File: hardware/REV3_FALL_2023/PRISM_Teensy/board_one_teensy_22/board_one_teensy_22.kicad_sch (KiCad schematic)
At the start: 20 parts, among them J2 PRISM_IO_INTERFACE, J3 3387, U1 Teensy4.0, U2 GPS-14414, U3 3966, U4 RFM69HCW_Breakout

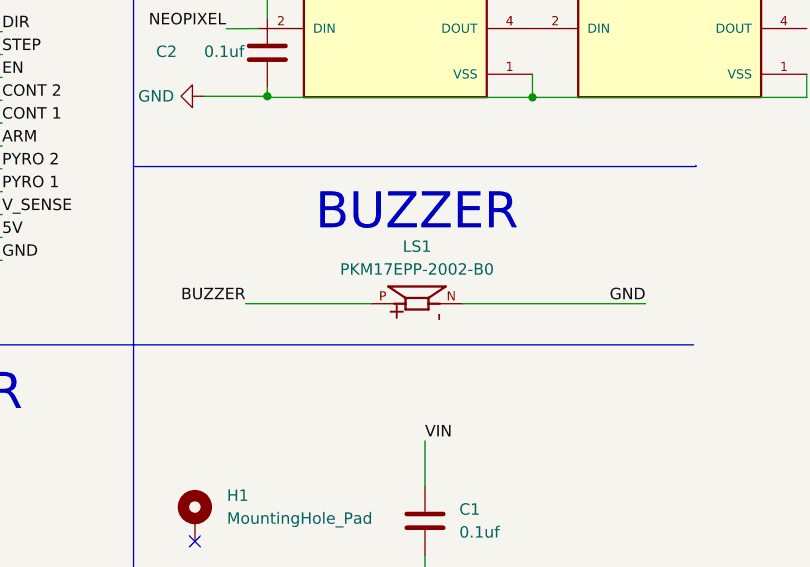
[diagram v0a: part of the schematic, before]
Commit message: created new symbol and footprint for buzzer
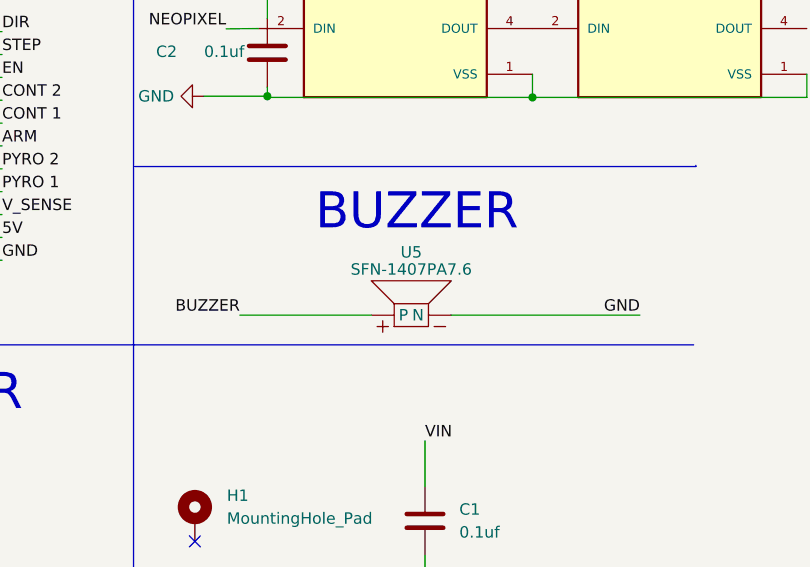
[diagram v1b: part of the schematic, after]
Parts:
- removed LS1: PKM17EPP-2002-B0, PKM17EPP-2002-B0:SPKR_PKM17EPP-2002-B0, symbol PKM:PKM17EPP-2002-B0
- added U5: SFN-1407PA7.6, buzzers:SFN-1407PA7.6, symbol SFN-1407PA7.6:SFN-1407PA7.6
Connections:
- net BUZZER: now also U5. (P)
- net GND: now also U5. (P)
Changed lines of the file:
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@@
     (stroke (width 0) (type default))
   )
-  (wire (pts (xy 279.4 66.04) (xy 259.08 66.04))
+  (wire (pts (xy 257.81 67.31) (xy 278.765 67.31))
     (stroke (width 0) (type default))
   )
@@
     (stroke (width 0) (type default))
   )
-  (wire (pts (xy 234.95 66.04) (xy 248.92 66.04))
+  (wire (pts (xy 234.315 67.31) (xy 248.92 67.31))
     (stroke (width 0) (type default))
   )
@@
     (effects (font (size 1.27 1.27)) (justify right bottom))
   )
-  (label "BUZZER" (at 234.95 66.04 180) (fields_autoplaced)
+  (label "BUZZER" (at 234.315 67.31 180) (fields_autoplaced)
     (effects (font (size 1.27 1.27)) (justify right bottom))
   )
@@
     (effects (font (size 1.27 1.27)) (justify left bottom))
   )
-  (label "GND" (at 279.4 66.04 180) (fields_autoplaced)
+  (label "GND" (at 278.765 67.31 180) (fields_autoplaced)
     (effects (font (size 1.27 1.27)) (justify right bottom))
   )
@@
         (path "/7a48c3b0-2761-409e-ae2f-7ebae3820225"
           (reference "D5") (unit 1)
+        )
+      )
+    )
+  )
+  (symbol (lib_id "SFN-1407PA7.6:SFN-1407PA7.6") (at 253.365 64.77 0) (unit 1)
+    (in_bom yes) (on_board yes) (dnp no)
+    (property "Reference" "U5" (at 253.365 60.325 0)
+      (effects (font (size 1.27 1.27)))
+    )
+    (property "Value" "SFN-1407PA7.6" (at 253.365 62.23 0)
+      (effects (font (size 1.27 1.27)))
+    )
+    (property "Footprint" "buzzers:SFN-1407PA7.6" (at 251.46 67.31 90)
+      (effects (font (size 1.27 1.27)) hide)
+    )
+    (property "Datasheet" "" (at 251.46 67.31 90)
+      (effects (font (size 1.27 1.27)) hide)
+    )
+    (pin "")
+    (pin "")
+    (instances
+      (project "board_one_teensy_22"
+        (path "/7a48c3b0-2761-409e-ae2f-7ebae3820225"
+          (reference "U5") (unit 1)
         )
       )
@@
         )
       )
-    )
-  )
-  (symbol (lib_id "PKM:PKM17EPP-2002-B0") (at 254 66.04 90) (unit 1)
-    (in_bom yes) (on_board yes) (dnp no) (fields_autoplaced)
-    (property "Reference" "LS1" (at 254 59.69 90)
-      (effects (font (size 1.27 1.27)))
-    )
-    (property "Value" "PKM17EPP-2002-B0" (at 254 62.23 90)
-      (effects (font (size 1.27 1.27)))
-    )
-    (property "Footprint" "PKM17EPP-2002-B0:SPKR_PKM17EPP-2002-B0" (at 254 66.04 0)
-      (effects (font (size 1.27 1.27)) (justify bottom) hide)
-    )
-    (property "Datasheet" "" (at 254 66.04 0)
-      (effects (font (size 1.27 1.27)) hide)
-    )
-    (property "MF" "Murata Electronics" (at 254 66.04 0)
-      (effects (font (size 1.27 1.27)) (justify bottom) hide)
-    )
-    (property "MAXIMUM_PACKAGE_HEIGHT" "9.8 mm" (at 254 66.04 0)
-      (effects (font (size 1.27 1.27)) (justify bottom) hide)
-    )
-    (property "Package" "Radial-2 Murata" (at 254 66.04 0)
-      (effects (font (size 1.27 1.27)) (justify bottom) hide)
-    )
-    (property "Price" "None" (at 254 66.04 0)
-      (effects (font (size 1.27 1.27)) (justify bottom) hide)
-    )
-    (property "Check_prices" "https://www.snapeda.com/parts/PKM17EPP-2002-B0/Murata+Electronics+North+America/view-part/?ref=eda" (at 254 66.04 0)
-      (effects (font (size 1.27 1.27)) (justify bottom) hide)
-    )
-    (property "STANDARD" "IPC-7351B" (at 254 66.04 0)
-      (effects (font (size 1.27 1.27)) (justify bottom) hide)
-    )
-    (property "PARTREV" "August 1, 2017" (at 254 66.04 0)
-      (effects (font (size 1.27 1.27)) (justify bottom) hide)
-    )
-    (property "SnapEDA_Link" "https://www.snapeda.com/parts/PKM17EPP-2002-B0/Murata+Electronics+North+America/view-part/?ref=snap" (at 254 66.04 0)
-      (effects (font (size 1.27 1.27)) (justify bottom) hide)
-    )
-    (property "MP" "PKM17EPP-2002-B0" (at 254 66.04 0)
-      (effects (font (size 1.27 1.27)) (justify bottom) hide)
-    )
-    (property "Purchase-URL" "https://www.snapeda.com/api/url_track_click_mouser/?unipart_id=293922&manufacturer=Murata Electronics&part_name=PKM17EPP-2002-B0&search_term=3v buzzer" (at 254 66.04 0)
-      (effects (font (size 1.27 1.27)) (justify bottom) hide)
-    )
-    (property "Description" "\nBuzzers Transducer, Externally Driven Piezo 3 V - 2kHz 70dB @ 3V, 10cm Through Hole PC Pins\n" (at 254 66.04 0)
-      (effects (font (size 1.27 1.27)) (justify bottom) hide)
-    )
-    (property "Availability" "In Stock" (at 254 66.04 0)
-      (effects (font (size 1.27 1.27)) (justify bottom) hide)
-    )
-    (property "MANUFACTURER" "Murata Electronics" (at 254 66.04 0)
-      (effects (font (size 1.27 1.27)) (justify bottom) hide)
-    )
-    (pin "N")
-    (pin "P")
-    (instances
-      (project "board_one_teensy_22"
-        (path "/7a48c3b0-2761-409e-ae2f-7ebae3820225"
-          (reference "LS1") (unit 1)
-        )
-      )
